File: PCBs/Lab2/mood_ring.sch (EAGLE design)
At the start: 5 parts

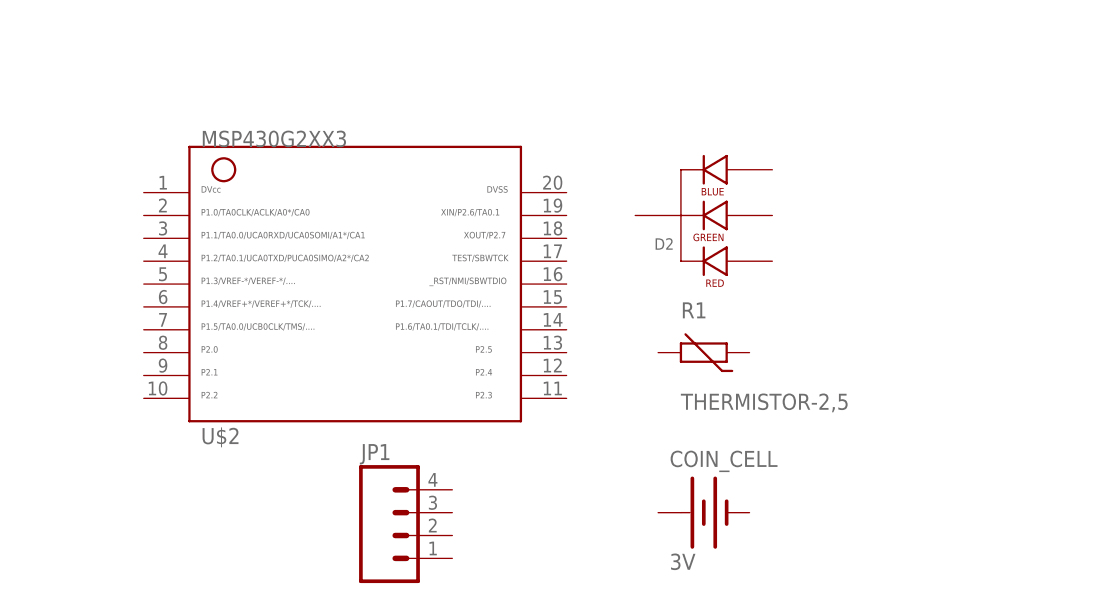
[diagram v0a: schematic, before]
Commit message: Updated skeleton file for lab 2 and updated library
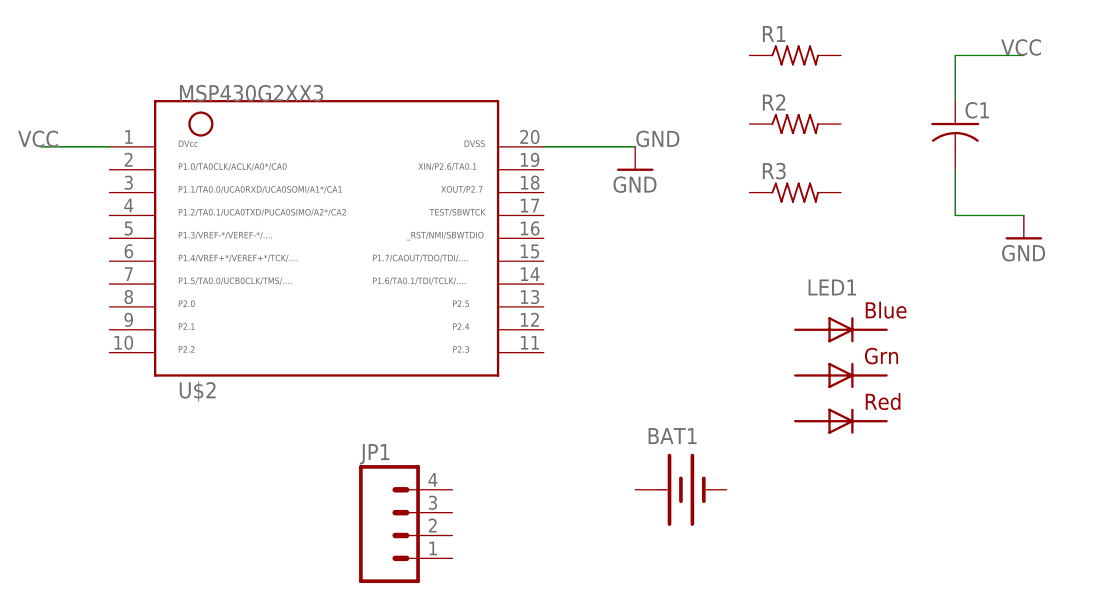
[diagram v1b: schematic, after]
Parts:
- removed COIN_CELL: 3V, ELEC327-lab2:BATTERY20PTH
- removed D2: LED-RGB-CCSMD, ELEC327-lab2:LED-RGB-CCSMD
- added BAT1: (no value), ELEC327:BATTERYBU2032SM
- added C1: (no value), resistor:C-USC1206
- added LED1: RGBLED5050, adafruit:RGBLED5050
- added R2, R3: (no value), resistor:R-US_R1206
- R1: value THERMISTOR-2,5 -> (none); device varistor:THERMISTOR-2,5 -> resistor:R-US_R1206
- U$2: value MSP430G2XX3TSSOP -> MSP430G2XX3PDIP; device ELEC327-lab2:MSP430G2XX3TSSOP -> ELEC327:MSP430G2XX3PDIP
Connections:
- new net GND: C1.2, U$2.20
- new net VCC: C1.1, U$2.1
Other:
- moved on the sheet: U$2
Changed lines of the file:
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@@
 <setting verticaltext="up"/>
 </settings>
-<grid distance="0.1" unitdist="inch" unit="inch" style="lines" multiple="1" display="no" altdistance="0.01" altunitdist="inch" altunit="inch"/>
+<grid distance="0.1" unitdist="inch" unit="inch" style="lines" multiple="1" display="yes" altdistance="0.01" altunitdist="inch" altunit="inch"/>
 <layers>
 <layer number="1" name="Top" color="4" fill="1" visible="no" active="no"/>
@@
 <layer number="54" name="bGND_GNDA" color="1" fill="9" visible="no" active="no"/>
 <layer number="56" name="wert" color="7" fill="1" visible="no" active="no"/>
+<layer number="57" name="tCAD" color="7" fill="1" visible="no" active="no"/>
 <layer number="59" name="tCarbon" color="7" fill="1" visible="no" active="no"/>
 <layer number="60" name="bCarbon" color="7" fill="1" visible="no" active="no"/>
@@
 <layer number="97" name="Info" color="7" fill="1" visible="yes" active="yes"/>
 <layer number="98" name="Guide" color="6" fill="1" visible="yes" active="yes"/>
+<layer number="99" name="SpiceOrder" color="7" fill="1" visible="no" active="no"/>
 <layer number="100" name="Muster" color="7" fill="1" visible="no" active="no"/>
 <layer number="101" name="Patch_Top" color="12" fill="4" visible="no" active="yes"/>
@@
 <layer number="111" name="Design_Info" color="7" fill="1" visible="yes" active="yes"/>
 <layer number="112" name="CC430_Restrict" color="7" fill="1" visible="yes" active="yes"/>
+<layer number="113" name="ReferenceLS" color="7" fill="1" visible="no" active="no"/>
 <layer number="116" name="Patch_BOT" color="9" fill="4" visible="no" active="yes"/>
+<layer number="118" name="Rect_Pads" color="7" fill="1" visible="no" active="no"/>
 <layer number="121" name="_tsilk" color="7" fill="1" visible="no" active="yes"/>
 <layer number="122" name="_bsilk" color="7" fill="1" visible="no" active="yes"/>
@@
 <layer number="132" name="bAdjust" color="7" fill="1" visible="yes" active="yes"/>
 <layer number="144" name="Drill_legend" color="7" fill="1" visible="no" active="yes"/>
+<layer number="150" name="Notes" color="7" fill="1" visible="no" active="yes"/>
 <layer number="151" name="HeatSink" color="7" fill="1" visible="no" active="yes"/>
 <layer number="152" name="_bDocu" color="7" fill="1" visible="yes" active="yes"/>
+<layer number="153" name="FabDoc1" color="6" fill="1" visible="no" active="no"/>
+<layer number="154" name="FabDoc2" color="2" fill="1" visible="no" active="no"/>
+<layer number="155" name="FabDoc3" color="7" fill="15" visible="no" active="no"/>
 <layer number="199" name="Contour" color="7" fill="1" visible="no" active="yes"/>
 <layer number="200" name="200bmp" color="1" fill="10" visible="no" active="yes"/>
@@
 <layer number="223" name="223bmp" color="24" fill="1" visible="no" active="no"/>
 <layer number="224" name="224bmp" color="25" fill="1" visible="no" active="no"/>
+<layer number="231" name="Eagle3D_PG1" color="7" fill="1" visible="no" active="no"/>
+<layer number="232" name="Eagle3D_PG2" color="7" fill="1" visible="no" active="no"/>
+<layer number="233" name="Eagle3D_PG3" color="7" fill="1" visible="no" active="no"/>
 <layer number="248" name="Housing" color="7" fill="1" visible="yes" active="yes"/>
 <layer number="249" name="Edge" color="7" fill="1" visible="yes" active="yes"/>
@@
 </classes>
 <parts>
-<part name="U$2" library="ELEC327-lab2" deviceset="MSP430G2XX3" device="TSSOP"/>
-<part name="D2" library="ELEC327-lab2" deviceset="LED-RGB-CC" device="SMD"/>
-<part name="R1" library="varistor" deviceset="THERMISTOR" device="-2,5"/>
-<part name="COIN_CELL" library="ELEC327-lab2" deviceset="BATTERY" device="20PTH" value="3V"/>
+<part name="U$2" library="ELEC327" deviceset="MSP430G2XX3" device="PDIP"/>
 <part name="JP1" library="SparkFun" deviceset="M04" device="LOCK"/>
+<part name="R1" library="resistor" deviceset="R-US_" device="R1206"/>
+<part name="R2" library="resistor" deviceset="R-US_" device="R1206"/>
+<part name="R3" library="resistor" deviceset="R-US_" device="R1206"/>
+<part name="LED1" library="adafruit" deviceset="RGBLED" device="5050"/>
+<part name="BAT1" library="ELEC327" deviceset="BATTERY" device="BU2032SM"/>
+<part name="C1" library="resistor" deviceset="C-US" device="C1206"/>
+<part name="GND1" library="supply1" deviceset="GND" device=""/>
+<part name="GND2" library="supply1" deviceset="GND" device=""/>
 </parts>
 <sheets>
@@
 </plain>
 <instances>
-<instance part="U$2" gate="G$1" x="-20.32" y="167.64"/>
-<instance part="D2" gate="G$1" x="20.32" y="172.72" rot="R180"/>
-<instance part="R1" gate="G$1" x="17.78" y="157.48"/>
-<instance part="COIN_CELL" gate="G$1" x="17.78" y="139.7"/>
+<instance part="U$2" gate="G$1" x="-22.86" y="172.72"/>
 <instance part="JP1" gate="G$1" x="-15.24" y="137.16"/>
+<instance part="R1" gate="G$1" x="27.94" y="190.5"/>
+<instance part="R2" gate="G$1" x="27.94" y="182.88"/>
+<instance part="R3" gate="G$1" x="27.94" y="175.26"/>
+<instance part="LED1" gate="G$1" x="33.02" y="154.94"/>
+<instance part="BAT1" gate="G$1" x="15.24" y="142.24"/>
+<instance part="C1" gate="G$1" x="45.72" y="182.88"/>
+<instance part="GND1" gate="1" x="10.16" y="177.8"/>
+<instance part="GND2" gate="1" x="53.34" y="170.18"/>
 </instances>
 <busses>
 </busses>
 <nets>
+<net name="VCC" class="0">
+<segment>
+<pinref part="U$2" gate="G$1" pin="1"/>
+<wire x1="-48.26" y1="180.34" x2="-55.88" y2="180.34" width="0.1524" layer="91"/>
+<label x="-58.42" y="180.34" size="1.778" layer="95"/>
+</segment>
+<segment>
+<pinref part="C1" gate="G$1" pin="1"/>
+<wire x1="45.72" y1="185.42" x2="45.72" y2="190.5" width="0.1524" layer="91"/>
+<wire x1="45.72" y1="190.5" x2="53.34" y2="190.5" width="0.1524" layer="91"/>
+<label x="50.8" y="190.5" size="1.778" layer="95"/>
+</segment>
+</net>
+<net name="GND" class="0">
+<segment>
+<pinref part="U$2" gate="G$1" pin="20"/>
+<wire x1="0" y1="180.34" x2="10.16" y2="180.34" width="0.1524" layer="91"/>
+<label x="10.16" y="180.34" size="1.778" layer="95"/>
+<pinref part="GND1" gate="1" pin="GND"/>
+</segment>
+<segment>
+<pinref part="C1" gate="G$1" pin="2"/>
+<wire x1="45.72" y1="177.8" x2="45.72" y2="172.72" width="0.1524" layer="91"/>
+<wire x1="45.72" y1="172.72" x2="53.34" y2="172.72" width="0.1524" layer="91"/>
+<pinref part="GND2" gate="1" pin="GND"/>
+</segment>
+</net>
 </nets>
 </sheet>

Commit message: added lab 2
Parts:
- added R4: (no value), resistor:R-US_R1206
- U$2: value MSP430G2XX3PDIP -> MSP430G2XX3TSSOP; device ELEC327:MSP430G2XX3PDIP -> ELEC327:MSP430G2XX3TSSOP
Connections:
- new net BLUE: R2.1, U$2.10
- new net GREEN: R4.1, U$2.4
- new net N$1: LED1.BLUE_A, R4.2
- new net N$2: LED1.GREEN_A, R3.2
- new net N$3: LED1.RED_A, R2.2
- new net RED: R3.1, U$2.13
- new net RST: JP1.3, R1.2, U$2.16
- new net TEST: JP1.2, U$2.17
- net GND: now also BAT1.-, JP1.4, LED1.BLUE_C, LED1.GREEN_C, LED1.RED_C
- net VCC: now also BAT1.+, JP1.1, R1.1
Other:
- moved on the sheet: BAT1, JP1, LED1, R1, R2, R3
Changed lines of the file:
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@@
 <?xml version="1.0" encoding="utf-8"?>
 <!DOCTYPE eagle SYSTEM "eagle.dtd">
-<eagle version="6.5.0">
+<eagle version="7.2.0">
 <drawing>
 <settings>
@@
 <setting verticaltext="up"/>
 </settings>
-<grid distance="0.1" unitdist="inch" unit="inch" style="lines" multiple="1" display="yes" altdistance="0.01" altunitdist="inch" altunit="inch"/>
+<grid distance="0.1" unitdist="inch" unit="inch" style="lines" multiple="1" display="no" altdistance="0.01" altunitdist="inch" altunit="inch"/>
 <layers>
 <layer number="1" name="Top" color="4" fill="1" visible="no" active="no"/>
@@
 </classes>
 <parts>
-<part name="U$2" library="ELEC327" deviceset="MSP430G2XX3" device="PDIP"/>
+<part name="U$2" library="ELEC327" deviceset="MSP430G2XX3" device="TSSOP" value="MSP430G2XX3TSSOP"/>
 <part name="JP1" library="SparkFun" deviceset="M04" device="LOCK"/>
 <part name="R1" library="resistor" deviceset="R-US_" device="R1206"/>
@@
 <part name="C1" library="resistor" deviceset="C-US" device="C1206"/>
 <part name="GND1" library="supply1" deviceset="GND" device=""/>
-<part name="GND2" library="supply1" deviceset="GND" device=""/>
+<part name="R4" library="resistor" deviceset="R-US_" device="R1206"/>
 </parts>
 <sheets>
@@
 <instances>
 <instance part="U$2" gate="G$1" x="-22.86" y="172.72"/>
-<instance part="JP1" gate="G$1" x="-15.24" y="137.16"/>
-<instance part="R1" gate="G$1" x="27.94" y="190.5"/>
-<instance part="R2" gate="G$1" x="27.94" y="182.88"/>
-<instance part="R3" gate="G$1" x="27.94" y="175.26"/>
-<instance part="LED1" gate="G$1" x="33.02" y="154.94"/>
-<instance part="BAT1" gate="G$1" x="15.24" y="142.24"/>
+<instance part="JP1" gate="G$1" x="17.78" y="157.48"/>
+<instance part="R1" gate="G$1" x="-15.24" y="149.86"/>
+<instance part="R2" gate="G$1" x="35.56" y="134.62"/>
+<instance part="R3" gate="G$1" x="33.02" y="139.7"/>
+<instance part="LED1" gate="G$1" x="48.26" y="139.7"/>
+<instance part="BAT1" gate="G$1" x="-15.24" y="137.16"/>
 <instance part="C1" gate="G$1" x="45.72" y="182.88"/>
 <instance part="GND1" gate="1" x="10.16" y="177.8"/>
-<instance part="GND2" gate="1" x="53.34" y="170.18"/>
+<instance part="R4" gate="G$1" x="33.02" y="144.78"/>
 </instances>
 <busses>
@@
 <net name="VCC" class="0">
 <segment>
+<pinref part="BAT1" gate="G$1" pin="+"/>
+<pinref part="R1" gate="G$1" pin="1"/>
+<wire x1="-20.32" y1="137.16" x2="-20.32" y2="149.86" width="0.1524" layer="91"/>
+<label x="-25.4" y="149.86" size="1.778" layer="95"/>
+<label x="-25.4" y="137.16" size="1.778" layer="95"/>
+</segment>
+<segment>
 <pinref part="U$2" gate="G$1" pin="1"/>
 <wire x1="-48.26" y1="180.34" x2="-55.88" y2="180.34" width="0.1524" layer="91"/>
@@
 </segment>
 <segment>
+<pinref part="JP1" gate="G$1" pin="1"/>
+<wire x1="22.86" y1="154.94" x2="25.4" y2="154.94" width="0.1524" layer="91"/>
+<label x="25.4" y="152.4" size="1.778" layer="95"/>
+</segment>
+<segment>
 <pinref part="C1" gate="G$1" pin="1"/>
-<wire x1="45.72" y1="185.42" x2="45.72" y2="190.5" width="0.1524" layer="91"/>
-<wire x1="45.72" y1="190.5" x2="53.34" y2="190.5" width="0.1524" layer="91"/>
-<label x="50.8" y="190.5" size="1.778" layer="95"/>
+<wire x1="45.72" y1="185.42" x2="45.72" y2="187.96" width="0.1524" layer="91"/>
+<label x="45.72" y="187.96" size="1.778" layer="95"/>
 </segment>
 </net>
 <net name="GND" class="0">
 <segment>
+<pinref part="GND1" gate="1" pin="GND"/>
 <pinref part="U$2" gate="G$1" pin="20"/>
 <wire x1="0" y1="180.34" x2="10.16" y2="180.34" width="0.1524" layer="91"/>
 <label x="10.16" y="180.34" size="1.778" layer="95"/>
-<pinref part="GND1" gate="1" pin="GND"/>
+</segment>
+<segment>
+<pinref part="LED1" gate="G$1" pin="BLUE_C"/>
+<wire x1="53.34" y1="144.78" x2="58.42" y2="144.78" width="0.1524" layer="91"/>
+<label x="53.34" y="147.32" size="1.778" layer="95"/>
+</segment>
+<segment>
+<pinref part="LED1" gate="G$1" pin="RED_C"/>
+<wire x1="53.34" y1="134.62" x2="58.42" y2="134.62" width="0.1524" layer="91"/>
+<label x="53.34" y="132.08" size="1.778" layer="95"/>
+</segment>
+<segment>
+<pinref part="BAT1" gate="G$1" pin="-"/>
+<wire x1="-10.16" y1="137.16" x2="-5.08" y2="137.16" width="0.1524" layer="91"/>
+<label x="-10.16" y="137.16" size="1.778" layer="95"/>
+</segment>
+<segment>
+<pinref part="JP1" gate="G$1" pin="4"/>
+<wire x1="22.86" y1="162.56" x2="27.94" y2="162.56" width="0.1524" layer="91"/>
+<label x="25.4" y="162.56" size="1.778" layer="95"/>
 </segment>
 <segment>
 <pinref part="C1" gate="G$1" pin="2"/>
 <wire x1="45.72" y1="177.8" x2="45.72" y2="172.72" width="0.1524" layer="91"/>
-<wire x1="45.72" y1="172.72" x2="53.34" y2="172.72" width="0.1524" layer="91"/>
-<pinref part="GND2" gate="1" pin="GND"/>
-</segment>
-</net>
+<label x="45.72" y="175.26" size="1.778" layer="95"/>
+</segment>
+<segment>
+<pinref part="LED1" gate="G$1" pin="GREEN_C"/>
+<wire x1="53.34" y1="139.7" x2="58.42" y2="139.7" width="0.1524" layer="91"/>
+<label x="55.88" y="139.7" size="1.778" layer="95"/>
+</segment>
+</net>
+<net name="RST" class="0">
+<segment>
+<pinref part="R1" gate="G$1" pin="2"/>
+<wire x1="-10.16" y1="149.86" x2="2.54" y2="149.86" width="0.1524" layer="91"/>
+<label x="-10.16" y="149.86" size="1.778" layer="95"/>
+</segment>
+<segment>
+<wire x1="0" y1="170.18" x2="7.62" y2="170.18" width="0.1524" layer="91"/>
+<pinref part="U$2" gate="G$1" pin="16"/>
+<label x="2.54" y="167.64" size="1.778" layer="95"/>
+</segment>
+<segment>
+<pinref part="JP1" gate="G$1" pin="3"/>
+<wire x1="22.86" y1="160.02" x2="27.94" y2="160.02" width="0.1524" layer="91"/>
+<label x="25.4" y="160.02" size="1.778" layer="95"/>
+</segment>
+</net>
+<net name="TEST" class="0">
+<segment>
+<pinref part="U$2" gate="G$1" pin="17"/>
+<wire x1="0" y1="172.72" x2="10.16" y2="172.72" width="0.1524" layer="91"/>
+<label x="2.54" y="172.72" size="1.778" layer="95"/>
+</segment>
+<segment>
+<pinref part="JP1" gate="G$1" pin="2"/>
+<wire x1="22.86" y1="157.48" x2="27.94" y2="157.48" width="0.1524" layer="91"/>
+<label x="27.94" y="157.48" size="1.778" layer="95"/>
+</segment>
+</net>
+<net name="RED" class="0">
+<segment>
+<pinref part="U$2" gate="G$1" pin="13"/>
+<wire x1="0" y1="162.56" x2="5.08" y2="162.56" width="0.1524" layer="91"/>
+<label x="2.54" y="160.02" size="1.778" layer="95"/>
+</segment>
+<segment>
+<pinref part="R3" gate="G$1" pin="1"/>
+<wire x1="25.4" y1="139.7" x2="27.94" y2="139.7" width="0.1524" layer="91"/>
+<label x="17.78" y="139.7" size="1.778" layer="95"/>
+</segment>
+</net>
+<net name="BLUE" class="0">
+<segment>
+<pinref part="U$2" gate="G$1" pin="10"/>
+<wire x1="-48.26" y1="157.48" x2="-53.34" y2="157.48" width="0.1524" layer="91"/>
+<label x="-45.72" y="154.94" size="1.778" layer="95" rot="R180"/>
+</segment>
+<segment>
+<pinref part="R2" gate="G$1" pin="1"/>
+<wire x1="30.48" y1="134.62" x2="25.4" y2="134.62" width="0.1524" layer="91"/>
+<label x="17.78" y="134.62" size="1.778" layer="95"/>
+</segment>
+</net>
+<net name="GREEN" class="0">
+<segment>
+<pinref part="U$2" gate="G$1" pin="4"/>
+<wire x1="-48.26" y1="172.72" x2="-55.88" y2="172.72" width="0.1524" layer="91"/>
+<label x="-58.42" y="170.18" size="1.778" layer="95"/>
+</segment>
+<segment>
+<pinref part="R4" gate="G$1" pin="1"/>
+<wire x1="27.94" y1="144.78" x2="20.32" y2="144.78" width="0.1524" layer="91"/>
+<label x="15.24" y="144.78" size="1.778" layer="95"/>
+</segment>
+</net>
+<net name="N$1" class="0">
+<segment>
+<pinref part="R4" gate="G$1" pin="2"/>
+<pinref part="LED1" gate="G$1" pin="BLUE_A"/>
+<wire x1="38.1" y1="144.78" x2="43.18" y2="144.78" width="0.1524" layer="91"/>
+</segment>
+</net>
+<net name="N$2" class="0">
+<segment>
+<pinref part="R3" gate="G$1" pin="2"/>
+<pinref part="LED1" gate="G$1" pin="GREEN_A"/>
+<wire x1="38.1" y1="139.7" x2="43.18" y2="139.7" width="0.1524" layer="91"/>
+</segment>
+</net>
+<net name="N$3" class="0">
+<segment>
+<pinref part="LED1" gate="G$1" pin="RED_A"/>
+<pinref part="R2" gate="G$1" pin="2"/>
+<wire x1="43.18" y1="134.62" x2="40.64" y2="134.62" width="0.1524" layer="91"/>
+</segment>
+</net>
